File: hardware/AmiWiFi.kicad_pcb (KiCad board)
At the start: 4 copper layers, 36.4 x 44.3 mm, 56 parts, among them J1 TYPE-C 6P, J2 DB25 MALE / MAS original, U1 LD2981ABU33TR, U2 SN74LVC4245APWR, U3 SN74LVC125APWR, U4 SN74LVC4245APWR, U5 SN74LVC1G10DBVR, U6 SN74LVC1G10DBVR, U7 Raspberry Pi Pico 2 W, U8 SN74LVC2G07DCKR

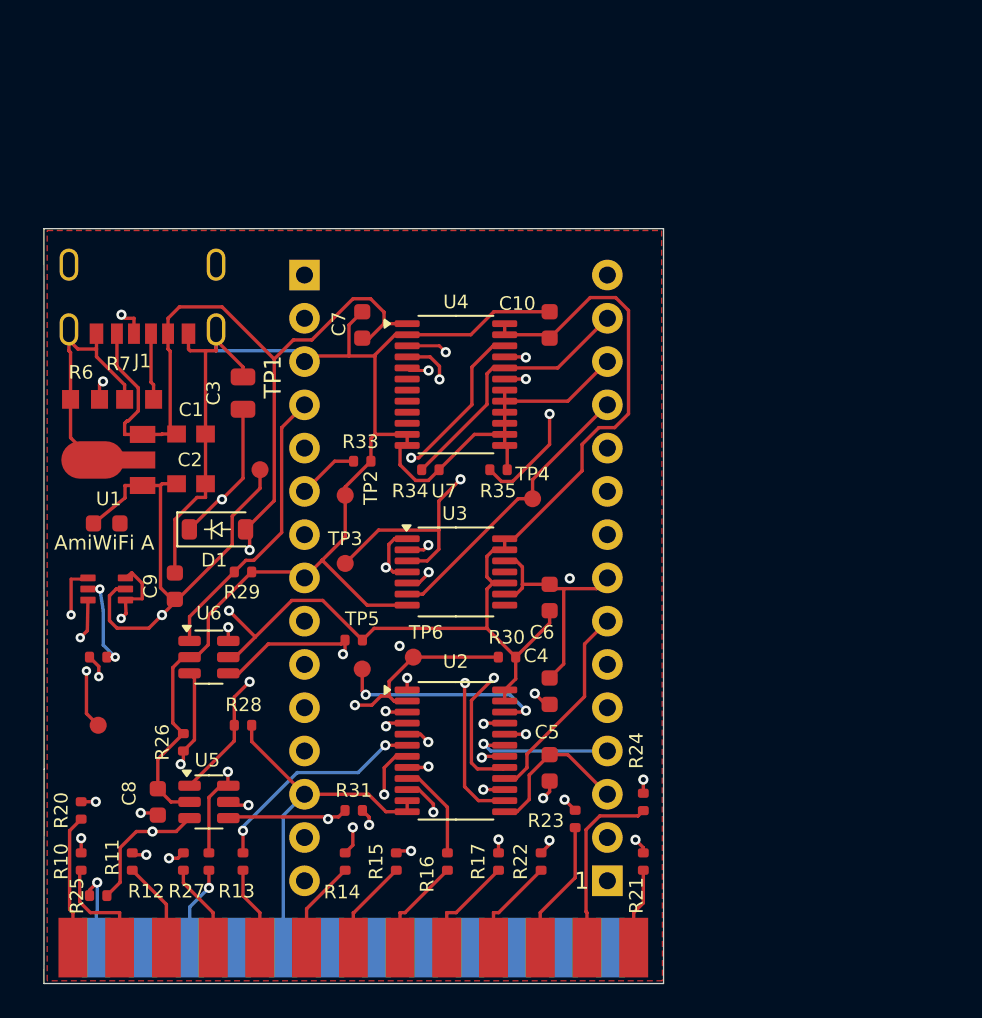
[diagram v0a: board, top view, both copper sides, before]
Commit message: Import user-edited KiCad files from AmiWiFi_Pico2W.zip
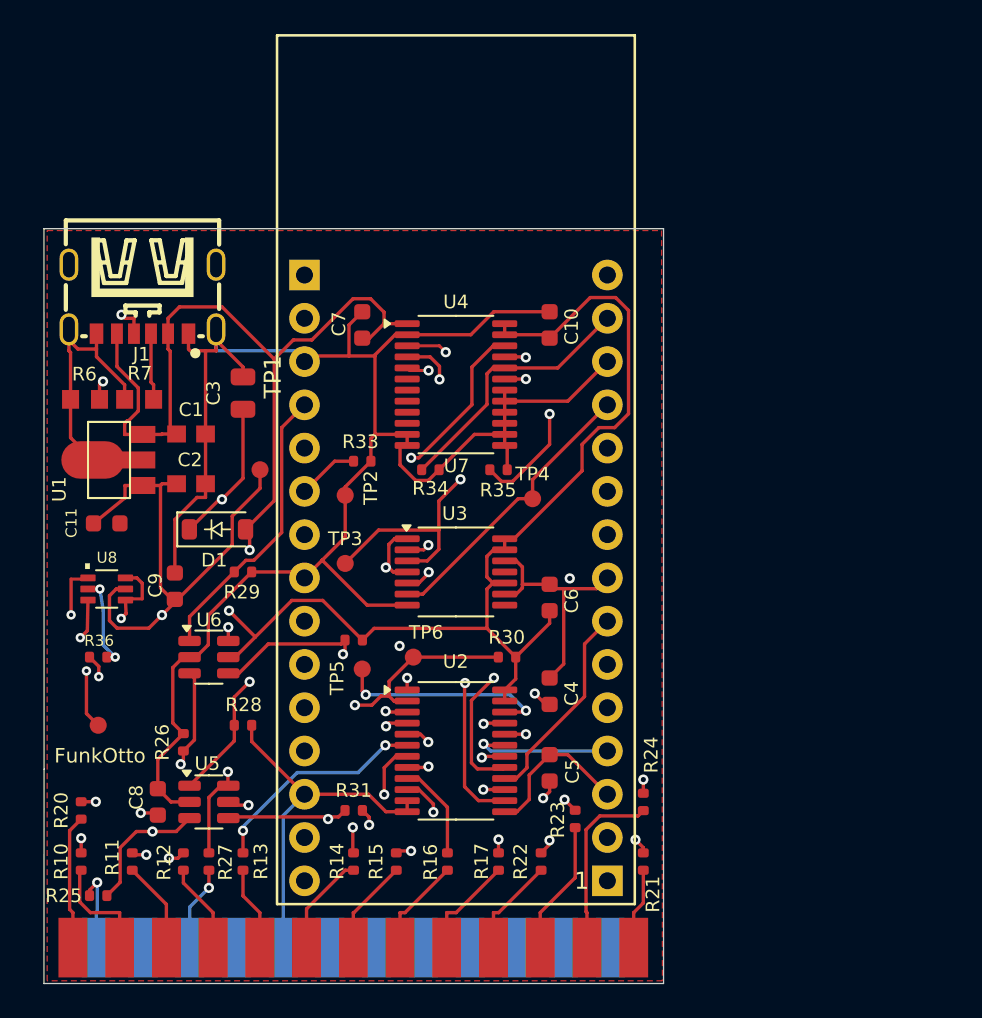
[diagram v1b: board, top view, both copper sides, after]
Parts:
- moved R14 0.49 mm to (148.5, 120.0)
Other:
- board text added: "."
- board text added: "FunkOtto"
- board text removed: "AmiWiFi A"

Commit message: Align KiCad footprints with user hardware revision and add missing LED components
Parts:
- added D2: LED, AmiWiFi:LED_0603_HandSolder_D2, F.Cu at (182.0, 102.0)
- added R18: 330, AmiWiFi:R0402_R18, F.Cu at (177.0, 102.0)
- moved TP7 4.78 mm to (136.0, 108.0)
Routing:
- net /PICO_RUN_N: track 26.5 -> 27.6 mm
- added copper zone on B.Cu, net /GND
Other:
- board text added: "Proto.1"
